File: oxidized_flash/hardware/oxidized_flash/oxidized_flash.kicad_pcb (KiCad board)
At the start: 2 copper layers, 36 parts, among them J1 USB_B_Micro, U1 LM1117-3.3, U2 ATSAMD51G18A-MU, U3 IS21ES, Y1 32.768

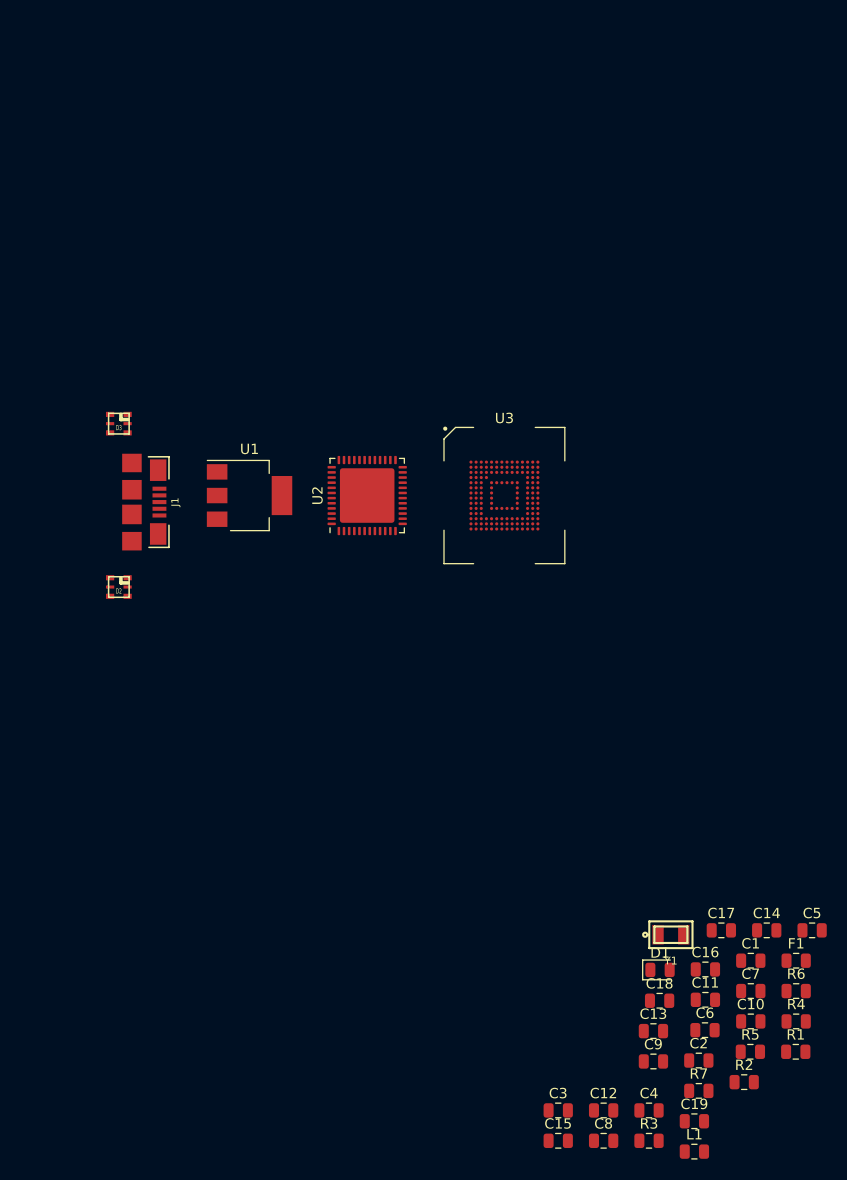
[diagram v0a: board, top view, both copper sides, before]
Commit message: Don't tie 3.3v directly to GND
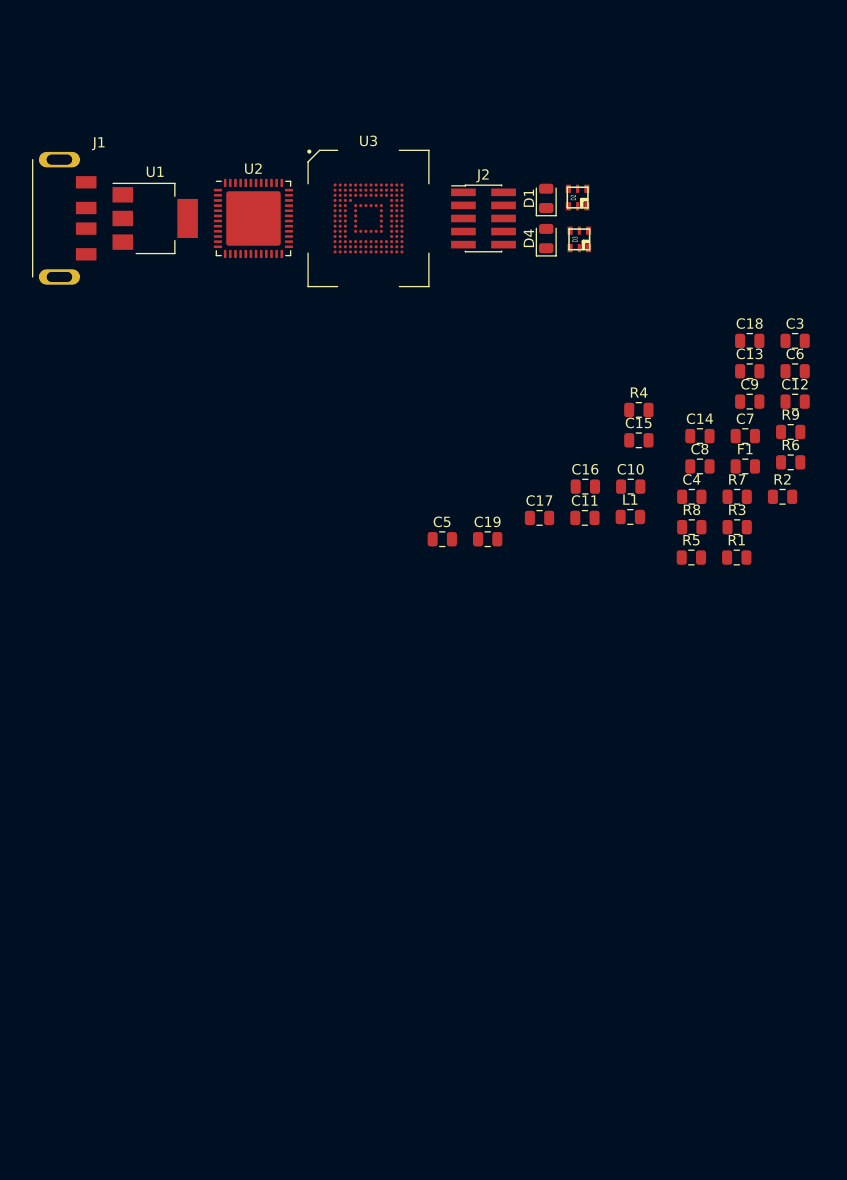
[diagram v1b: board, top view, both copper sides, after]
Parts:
- removed C1, C2: 22p, Capacitor_SMD:C_0805_2012Metric
- removed Y1: 32.768, Custom_Crystal:ECS-31B_xtal
- added D4: PWR_LED, LED_SMD:LED_0805_2012Metric, F.Cu at (75.2, 33.4)
- added J2: Conn_ARM_JTAG_SWD_10, Connector_PinHeader_1.27mm:PinHeader_2x05_P1.27mm_Vertical_SMD, F.Cu at (69.1, 31.5)
- added R8: 1k, Resistor_SMD:R_0805_2012Metric, F.Cu at (89.3, 61.5)
- added R9: 10k, Resistor_SMD:R_0805_2012Metric, F.Cu at (98.9, 52.2)
- D1: value LED_Small -> OK_Led
- J1: value USB_B_Micro -> USB_A; footprint Custom_USB:USB-MICRO-B-FCI-10118192 -> Custom_USB:Molex_48037_USB_A_Male
- R2: value 10k -> 1k
- moved C3 78.2 mm to (99.4, 43.4)
- moved D1 75.8 mm to (75.2, 29.5), turned to 90 degrees
- moved C12 71.3 mm to (99.4, 49.3)
- moved C15 68.5 mm to (84.2, 53.1)
- moved C8 66.2 mm to (90.1, 55.6)
- moved C13 64.8 mm to (95.0, 46.3)
- moved C9 64.8 mm to (95.0, 49.3)
- moved C18 64.7 mm to (95.0, 43.4)
- moved C6 64.6 mm to (99.4, 46.3)
- moved L1 62.0 mm to (83.4, 60.5)
- moved R4 61.4 mm to (84.2, 50.1)
- moved R3 60.2 mm to (93.7, 61.5)
- moved C19 60.0 mm to (69.5, 62.7)
- moved C4 59.8 mm to (89.3, 58.5)
- moved D2 58.5 mm to (78.2, 29.5), turned to 270 degrees
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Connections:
- net Net-(C3-Pad1) renamed /SWD_RST
- C10 pad 2: +3V3 -> GND
- C11 pad 2: +3V3 -> GND
- C12 pad 2: +3V3 -> GND
- C13 pad 2: +3V3 -> GND
- C14 pad 2: +3V3 -> GND
- C15 pad 2: +3V3 -> GND
- C16 pad 2: +3V3 -> GND
- C17 pad 2: +3V3 -> GND
- C18 pad 2: +3V3 -> GND
- C19 pad 2: +3V3 -> GND
- C3 pad 2: +3V3 -> GND
- C4 pad 2: +3V3 -> GND
- C5 pad 2: +3V3 -> GND
- C6 pad 2: +3V3 -> GND
- C7 pad 2: +3V3 -> GND
- C8 pad 2: +3V3 -> GND
- C9 pad 2: +3V3 -> GND
- D2 pad 3: +3V3 -> GND
- D3 pad 3: +3V3 -> GND
- J1 pad 4: Net-(J1-Pad4) -> GND
- J1 pad 5: +3V3 -> GND
- R1 pad 2: +3V3 -> GND
- U1 pad 1: +3V3 -> GND
- U2 pad 18: +3V3 -> GND
- U2 pad 35: +3V3 -> GND
- U2 pad 42: +3V3 -> GND
- U2 pad 45: Net-(U2-Pad45) -> /SWD_CLK
- U2 pad 46: Net-(U2-Pad46) -> /SWD_IO
- U2 pad 5: +3V3 -> GND
- U3 pad C4: +3V3 -> GND
- U3 pad E7: +3V3 -> GND
- U3 pad G5: +3V3 -> GND
- U3 pad H10: +3V3 -> GND
- U3 pad J5: +3V3 -> GND
- U3 pad K8: +3V3 -> GND
- U3 pad N2: +3V3 -> GND
- U3 pad N5: +3V3 -> GND
- U3 pad P4: +3V3 -> GND
- U3 pad P6: +3V3 -> GND
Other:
- net class Default: clearance 0.2 -> 0.127; via_dia 0.8 -> 0.6; via_drill 0.4 -> 0.3
- rule pad_to_mask_clearance: 0.051 -> 0.0508
- rule solder_mask_min_width: 0.25 -> 0.127
- rule trace_clearance: 0.2 -> 0.127

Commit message: Get passives close to their counterparts
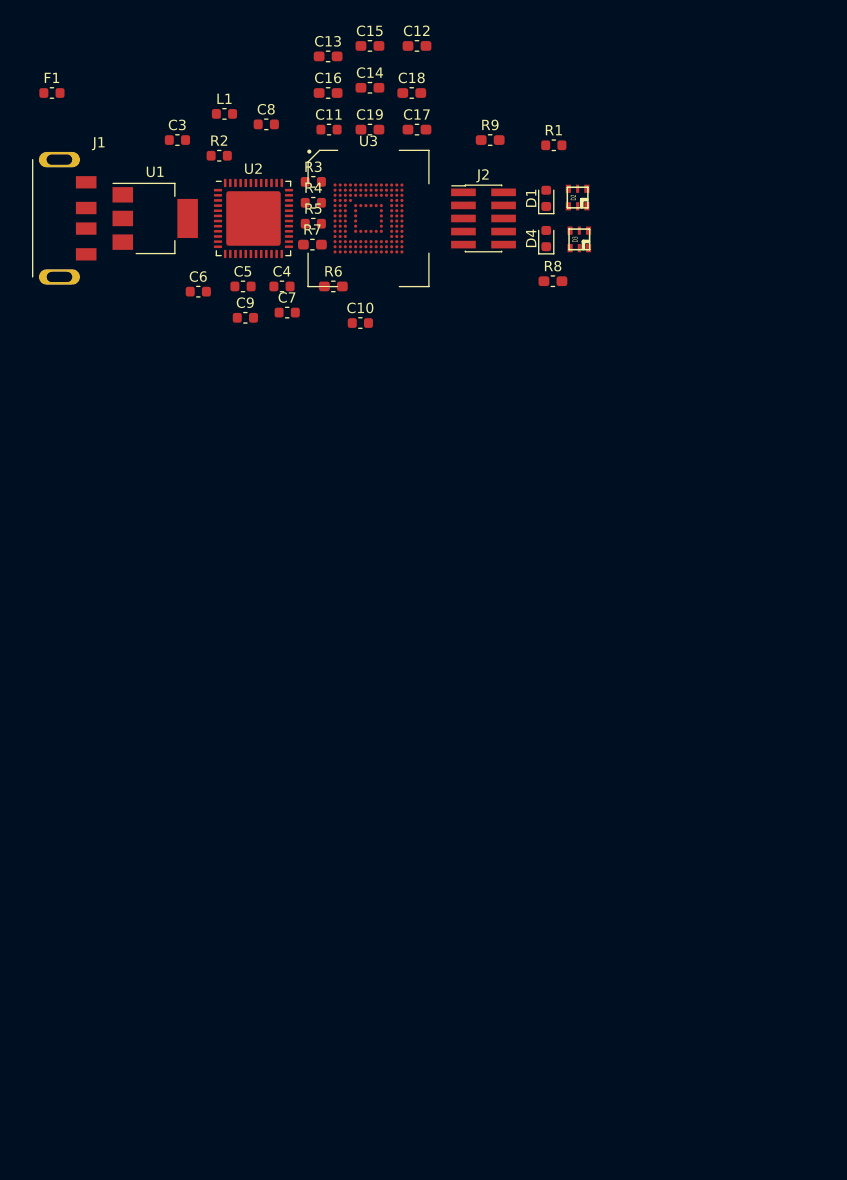
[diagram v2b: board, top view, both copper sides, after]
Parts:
- C10, C11, C3, C4, C5, C6, C7, C8, C9: footprint Capacitor_SMD:C_0805_2012Metric -> Capacitor_SMD:C_0603_1608Metric
- C12, C13, C14, C15, C16, C17, C18, C19: footprint Capacitor_SMD:C_0805_2012Metric -> Capacitor_SMD:C_0603_1608Metric_Pad1.05x0.95mm_HandSolder
- D1, D4: footprint LED_SMD:LED_0805_2012Metric -> LED_SMD:LED_0603_1608Metric
- F1: footprint Fuse:Fuse_0805_2012Metric -> Fuse:Fuse_0603_1608Metric
- L1: footprint Inductor_SMD:L_0805_2012Metric -> Inductor_SMD:L_0603_1608Metric
- R1, R2, R3, R4, R5: footprint Resistor_SMD:R_0805_2012Metric -> Resistor_SMD:R_0603_1608Metric
- R6, R7, R8, R9: footprint Resistor_SMD:R_0805_2012Metric -> Resistor_SMD:R_0603_1608Metric_Pad1.05x0.95mm_HandSolder
- moved F1 76.5 mm to (27.2, 19.3)
- moved R2 64.0 mm to (43.4, 25.4)
- moved C3 63.1 mm to (39.3, 23.9)
- moved C6 58.5 mm to (41.4, 38.6)
- moved L1 55.6 mm to (43.9, 21.3)
- moved C8 53.7 mm to (48.0, 22.4)
- moved R3 53.1 mm to (52.6, 27.9)
- moved C13 51.1 mm to (54.0, 15.7)
- moved C12 50.4 mm to (62.6, 14.7)
- moved C9 49.7 mm to (45.9, 41.1)
- moved R5 49.0 mm to (52.6, 32.0)
- moved R7 48.0 mm to (52.5, 34.0)
- moved R6 47.6 mm to (54.5, 38.1)
- moved C14 46.6 mm to (58.1, 18.8)
- moved C15 46.4 mm to (58.1, 14.7)
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
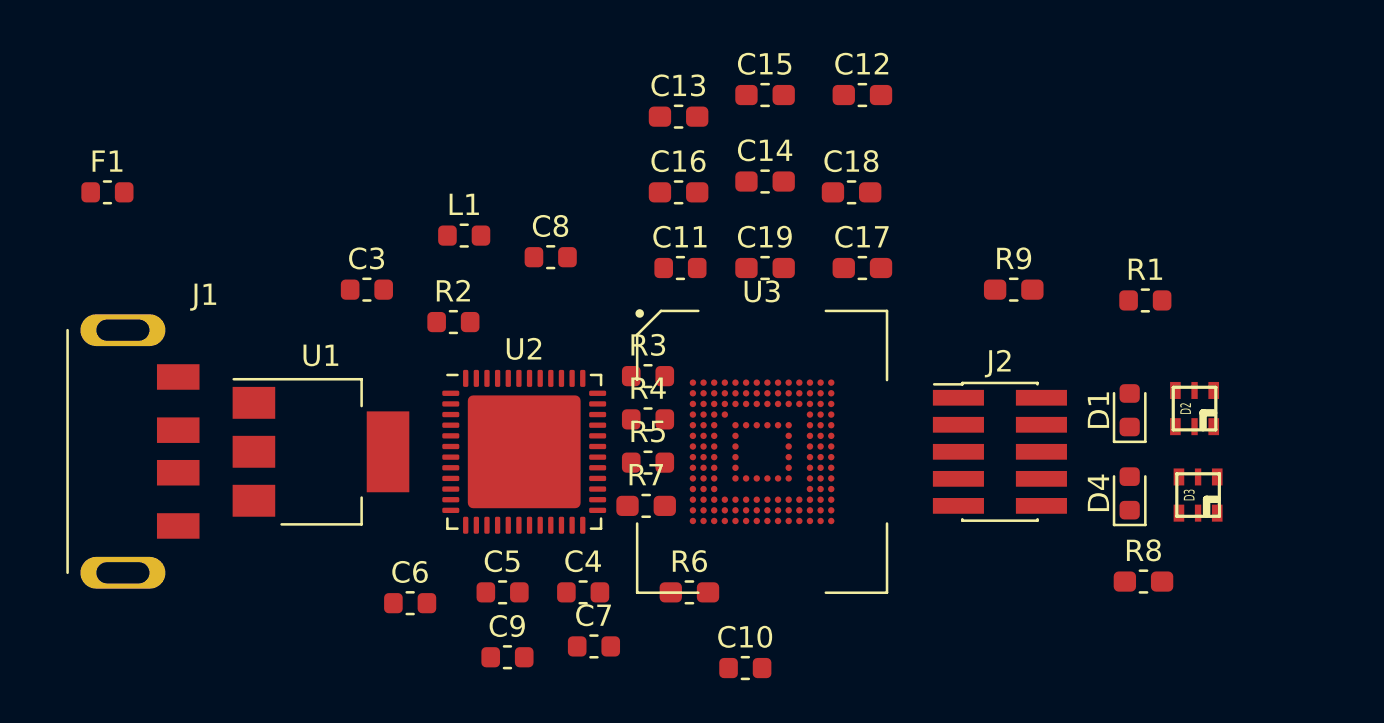
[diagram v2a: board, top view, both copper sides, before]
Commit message: Start initial track routing
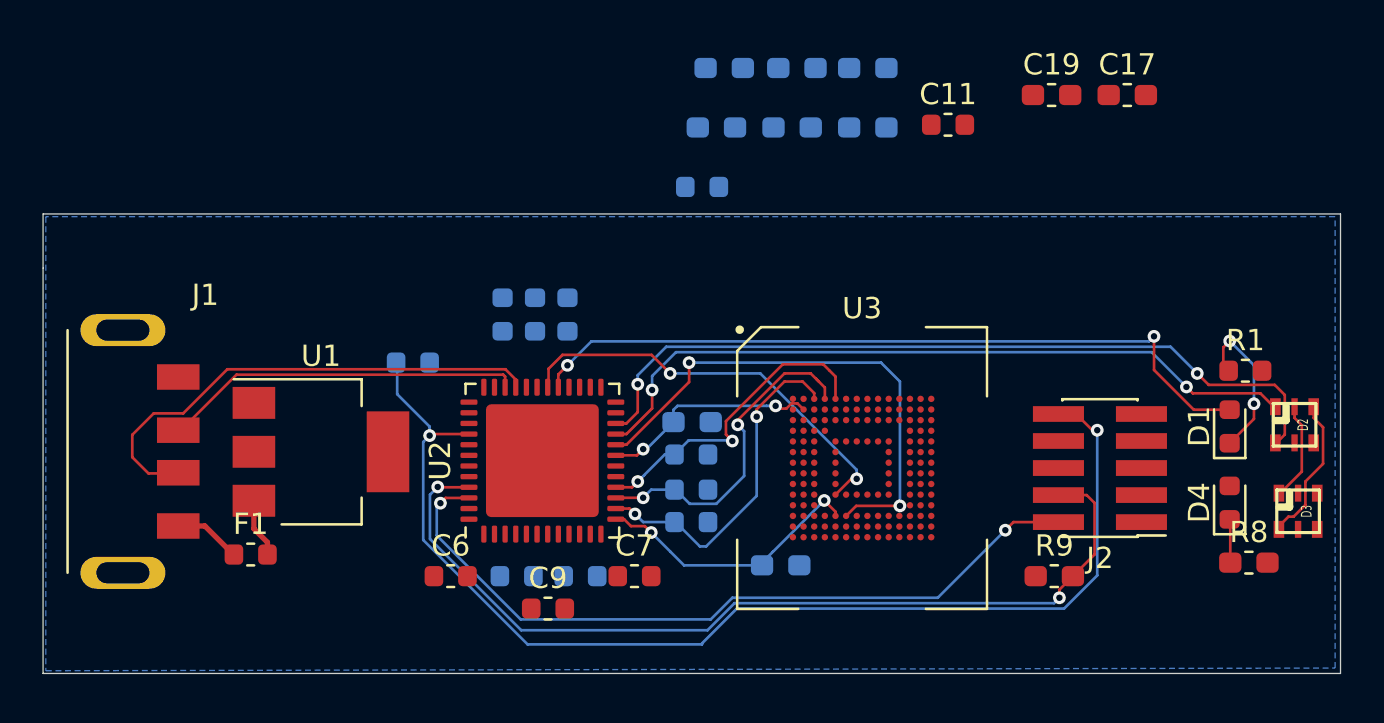
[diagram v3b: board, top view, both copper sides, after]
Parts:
- C10, C12, C13, C14, C15, C16, C18, C3, C4, C5, C8, L1, R2, R3, R4, R5, R6, R7: moved to B.Cu
- moved C10 22.7 mm to (55.1, 19.1), turned to 180 degrees
- moved F1 18.3 mm to (33.9, 36.3)
- moved C19 15.7 mm to (71.5, 14.7)
- moved C17 14.9 mm to (75.1, 14.7)
- moved C11 14.3 mm to (66.6, 16.1)
- moved R9 13.6 mm to (71.6, 37.3)
- moved C13 9.18 mm to (62.9, 13.5)
- moved R3 7.15 mm to (54.6, 34.8), turned to 180 degrees
- moved R1 5.74 mm to (80.6, 27.7)
- moved R8 5.03 mm to (80.8, 36.7)
- moved L1 4.98 mm to (47.2, 25.0), turned to 90 degrees
- moved J2 4.76 mm to (73.8, 32.3), turned to 180 degrees
- moved D1 4.76 mm to (79.9, 30.3)
- moved D2 4.76 mm to (82.9, 30.2), turned to 90 degrees
- moved D3 4.76 mm to (83.1, 34.3), turned to 90 degrees
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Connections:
- U2 pad 30: Net-(U2-Pad30) -> /MC_RST
- U3 pad K5: Net-(U3-PadK5) -> /MC_RST
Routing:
- net /SWD_RST: track 0.00 -> 55.0 mm, vias 0 -> 2
- net /SWD_CLK: track 0.00 -> 43.2 mm, vias 0 -> 2
- net /SCK: track 0.00 -> 37.3 mm, vias 0 -> 2
- net /SWD_IO: track 0.00 -> 35.8 mm, vias 0 -> 2
- net /PA20: track 0.00 -> 35.2 mm, vias 0 -> 2
- net /MOSI: track 0.00 -> 34.6 mm, vias 0 -> 2
- net Net-(U2-Pad20): track 0.00 -> 24.4 mm, vias 0 -> 2
- net Net-(J1-Pad2): track 0.00 -> 23.9 mm
- net /MC_RST: track 0.00 -> 19.7 mm, vias 0 -> 2
- net Net-(J1-Pad3): track 0.00 -> 17.0 mm
- net Net-(R3-Pad2): track 0.00 -> 16.1 mm, vias 0 -> 2
- net Net-(R4-Pad2): track 0.00 -> 15.8 mm, vias 0 -> 2
- net Net-(R5-Pad2): track 0.00 -> 14.9 mm, vias 0 -> 2
- net Net-(R6-Pad2): track 0.00 -> 13.3 mm, vias 0 -> 2
- net Net-(R7-Pad2): track 0.00 -> 10.4 mm, vias 0 -> 2
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- added copper zone on B.Cu, net GND
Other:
- board outline added: 61 x 21.6 mm
- net class BGA added: clearance 0, trace_width 0.25, via_dia 0.6, via_drill 0.3
